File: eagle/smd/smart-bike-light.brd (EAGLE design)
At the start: 66 x 18.7 mm, 12 parts, among them IC1 LM2936MP-3.3, Q1 FDN360P, U1 ADXL362, U2 AL8805WS

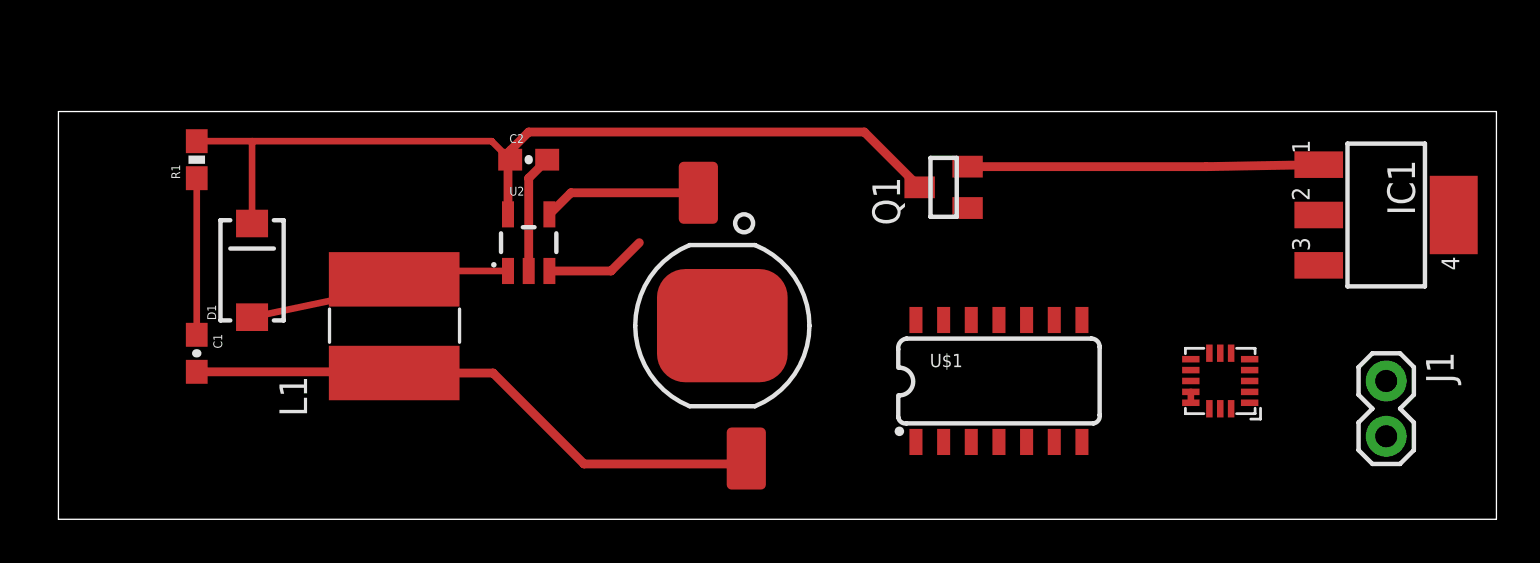
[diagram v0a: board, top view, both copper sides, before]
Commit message: switched to analog accel
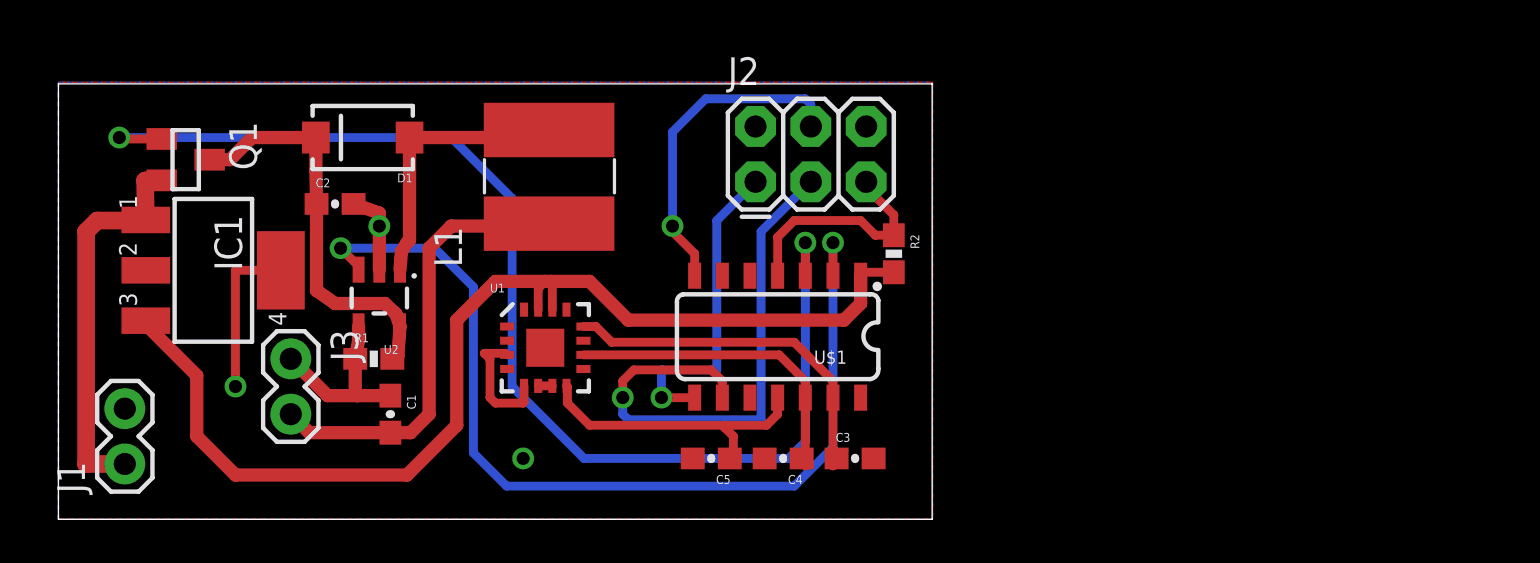
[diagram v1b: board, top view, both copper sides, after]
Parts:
- removed U$2: LUXEONSMD, SparkFun-LED:LUXEON
- added C3, C4, C5: 0.1uF, SparkFun-Capacitors:0603-CAP
- added J2: FEMALE 2x3, SparkFun-Connectors:2X3
- added J3: (no value), SparkFun-Connectors:1X02
- added R2: 20K, SparkFun-Resistors:0603-RES
- U1: value ADXL362 -> ADXL335; device SparkFun-Sensors:ADXL362 -> SparkFun-Sensors:LFCSP-16
- moved J1 58.0 mm to (3.05, 2.54), turned to 90 degrees
- moved IC1 53.9 mm to (7.11, 11.4)
- moved Q1 34.8 mm to (5.84, 16.5), turned to 270 degrees
- moved U1 31.0 mm to (22.4, 7.87), turned to 0 degrees
- moved R1 12.2 mm to (14.5, 7.37), turned to 0 degrees
- moved U$1 10.4 mm to (33.0, 8.38), turned to 180 degrees
- moved L1 9.88 mm to (22.4, 15.7)
- moved C1 9.32 mm to (15.2, 4.83)
- moved C2 9.12 mm to (12.7, 14.5)
- moved D1 7.94 mm to (14.0, 17.5), turned to 180 degrees
- moved U2 7.31 mm to (14.7, 10.2), turned to 180 degrees
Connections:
- removed net INT1: U$1.5, U1.P$11
- removed net INT2: U$1.3, U1.P$9
- new net AVR_MISO: J2.1, U$1.8
- new net AVR_MOSI: J2.4, U$1.7
- new net AVR_RST: J2.5, R2.1, U$1.4
- new net AVR_SCK: J2.3, U$1.9
- net 3V3: now also R2.2, U1.14, U1.15; no longer U1.P$1, U1.P$14
- net BRI_CTRL: now also U$1.2; no longer U$1.7, U1.P$6
- net GND: now also C3.2, C4.2, C5.2, J2.6, U1.3, U1.5, U1.6, U1.7; no longer U1.P$12, U1.P$13, U1.P$16
- net LED_EN: now also U$1.3; no longer U$1.13
- net N$1: now also J3.1; no longer U$2.A
- net N$4: now also J3.2; no longer U$2.C
- net N$5: now also C3.1, U$1.13, U1.12; no longer U$1.8, U1.P$7
- net N$6: now also C4.1, U$1.12, U1.10; no longer U$1.9, U1.P$4
- net N$7: now also C5.1, U$1.11, U1.8; no longer U$1.10, U1.P$8
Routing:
- net LED_EN: track 0.00 -> 55.6 mm, vias 0 -> 2
- net 3V3: track 0.00 -> 50.9 mm
- net BRI_CTRL: track 4.67 -> 44.6 mm, vias 0 -> 2
- net AVR_SCK: track 0.00 -> 25.6 mm, vias 0 -> 1
- net N$2: track 41.7 -> 18.6 mm
- net N$5: track 0.00 -> 16.8 mm
- net AVR_MOSI: track 0.00 -> 15.1 mm, vias 0 -> 1
- net N$6: track 0.00 -> 15.0 mm
- net AVR_MISO: track 0.00 -> 14.7 mm, vias 0 -> 1
- net N$7: track 0.00 -> 13.6 mm
- net GND: track 5.96 -> 17.6 mm, vias 0 -> 3
- net AVR_RST: track 0.00 -> 10.7 mm
- net N$4: track 27.1 -> 20.6 mm
- net N$1: track 14.4 -> 8.51 mm
- net VIN: track 16.1 -> 18.0 mm
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- added copper zone on layer 1, net GND
- added copper zone on layer 16, net GND
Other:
- board size 66 x 18.7 mm -> 40.1 x 20 mm

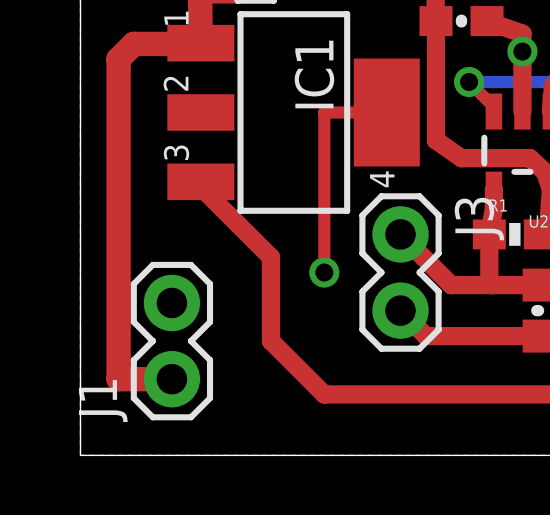
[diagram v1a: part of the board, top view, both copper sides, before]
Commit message: updated jumper silkscreens, README
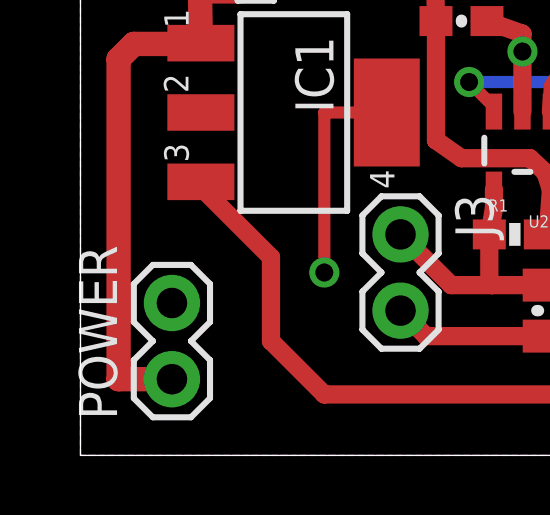
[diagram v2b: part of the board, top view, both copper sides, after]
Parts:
- renumbered J1 to POWER
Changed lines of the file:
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@@
 <wire x1="40.112" y1="19.99" x2="0" y2="19.99" width="0" layer="20"/>
 <wire x1="0" y1="19.99" x2="0" y2="0" width="0" layer="20"/>
-<dimension x1="0" y1="22.53" x2="39.878" y2="22.606" x3="19.92825625" y3="28.203903125" textsize="1.778" layer="1"/>
 <dimension x1="0" y1="19.99" x2="0" y2="0" x3="-1.524" y3="9.995" textsize="1.778" layer="1"/>
+<dimension x1="0" y1="20.066" x2="40.132" y2="20.066" x3="20.066" y3="22.098" textsize="1.778" layer="1"/>
 </plain>
 <attributes>
@@
 <attribute name="OC_NEWARK" value="41K4523" x="7.112" y="11.43" size="1.778" layer="27" rot="R270" display="off"/>
 </element>
-<element name="J1" library="SparkFun-Connectors" package="1X02" value="" x="3.048" y="2.54" rot="R90"/>
+<element name="POWER" library="SparkFun-Connectors" package="1X02" value="" x="3.048" y="2.54" rot="R90"/>
 <element name="J2" library="SparkFun-Connectors" package="2X3" value="FEMALE 2x3" x="32.004" y="15.494">
 <attribute name="PROD_ID" value="CONN-11566" x="32.004" y="15.494" size="1.778" layer="27" display="off"/>
@@
 <contactref element="C2" pad="2"/>
 <contactref element="U2" pad="2"/>
-<contactref element="J1" pad="2"/>
+<contactref element="POWER" pad="2"/>
 <contactref element="IC1" pad="2"/>
 <contactref element="IC1" pad="4"/>
@@
 </signal>
 <signal name="VIN">
-<contactref element="J1" pad="1"/>
+<contactref element="POWER" pad="1"/>
 <contactref element="Q1" pad="2"/>
 <contactref element="IC1" pad="1"/>
